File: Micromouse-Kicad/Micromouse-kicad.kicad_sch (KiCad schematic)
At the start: 101 parts, among them J1 SWD, J2 USB_B_Micro, J3 UARTBTH, J4 Batería, J5 VL6180x, J6 MotorEncodL, J7 MotorEncodR, Q1 BS170, Q2 BS170, Q3 BS170, Q4 BS170, SW1 RST, SW2 BootSwitch, SW3 PowerSwitch, SW4 BTN, SW5 BTN, U1 STM32F405RGT6, U10 TCRT5000, U2 AMS1117-5.0, U3 AMS1117-3.3, U4 SRV05-4, U5 MPU-6500, U6 DRV8833PWPR, U7 TCRT5000, U8 TCRT5000, U9 TCRT5000, Y1 8MHz

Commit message: PCB Completa - Depurada
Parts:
- removed DL1: ROJO, LED_SMD:LED_0603_1608Metric, symbol Device:LED
- removed DL3: VERDE, LED_SMD:LED_0603_1608Metric, symbol Device:LED
- removed R2: 220, Resistor_SMD:R_0603_1608Metric, symbol Device:R_Small
- removed RX1: 750, Resistor_SMD:R_0603_1608Metric, symbol Device:R_Small
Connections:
- net LED1: no longer names the net of U1.39 (PC8)
- net LED6: no longer names the net of U1.43 (PA10)
- no-connect marks 37 -> 39
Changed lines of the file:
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@@
   (no_connect (at 200.66 49.53))
   (no_connect (at 200.66 36.83))
+  (no_connect (at 114.3 81.28))
+  (no_connect (at 114.3 71.12))
   (no_connect (at 256.54 92.71))
   (no_connect (at 154.94 96.52))
@@
     )
   )
-  (global_label "LED6" (shape input) (at 114.3 81.28 0) (fields_autoplaced)
-    (effects (font (size 1.27 1.27)) (justify left))
-    (property "Intersheet References" "${INTERSHEET_REFS}" (id 0) (at 121.3698 81.2006 0)
-      (effects (font (size 1.27 1.27)) (justify left) hide)
-    )
-  )
   (global_label "Boton" (shape input) (at 83.82 83.82 180) (fields_autoplaced)
     (effects (font (size 1.27 1.27)) (justify right))
@@
     )
   )
-  (global_label "LED1" (shape input) (at 114.3 71.12 0) (fields_autoplaced)
-    (effects (font (size 1.27 1.27)) (justify left))
-    (property "Intersheet References" "${INTERSHEET_REFS}" (id 0) (at 121.3698 71.0406 0)
-      (effects (font (size 1.27 1.27)) (justify left) hide)
-    )
-  )
   (global_label "SWDIO" (shape input) (at 38.1 138.43 180) (fields_autoplaced)
     (effects (font (size 1.27 1.27)) (justify right))
@@
     )
   )
-  (global_label "LED1" (shape input) (at 17.78 177.8 90) (fields_autoplaced)
-    (effects (font (size 1.27 1.27)) (justify left))
-    (property "Intersheet References" "${INTERSHEET_REFS}" (id 0) (at 17.7006 170.7302 90)
-      (effects (font (size 1.27 1.27)) (justify left) hide)
-    )
-  )
   (global_label "OutML1" (shape input) (at 271.78 73.66 0) (fields_autoplaced)
     (effects (font (size 1.27 1.27)) (justify left))
@@
     )
   )
-  (global_label "LED6" (shape input) (at 43.18 177.8 90) (fields_autoplaced)
-    (effects (font (size 1.27 1.27)) (justify left))
-    (property "Intersheet References" "${INTERSHEET_REFS}" (id 0) (at 43.1006 170.7302 90)
-      (effects (font (size 1.27 1.27)) (justify left) hide)
-    )
-  )
   (global_label "I2C2_SCL" (shape input) (at 74.93 97.79 180) (fields_autoplaced)
     (effects (font (size 1.27 1.27)) (justify right))
@@
     (pin "2")
   )
-  (symbol (lib_id "power:GND") (at 43.18 190.5 0) (unit 1)
-    (in_bom yes) (on_board yes) (fields_autoplaced)
-    (property "Reference" "#PWR012" (id 0) (at 43.18 196.85 0)
-      (effects (font (size 1.27 1.27)) hide)
-    )
-    (property "Value" "GND" (id 1) (at 43.18 195.58 0))
-    (property "Footprint" "" (id 2) (at 43.18 190.5 0)
-      (effects (font (size 1.27 1.27)) hide)
-    )
-    (property "Datasheet" "" (id 3) (at 43.18 190.5 0)
-      (effects (font (size 1.27 1.27)) hide)
-    )
-    (pin "1")
-  )
   (symbol (lib_id "power:GND") (at 149.86 190.5 0) (unit 1)
     (in_bom yes) (on_board yes) (fields_autoplaced)
@@
     (pin "2")
   )
-  (symbol (lib_id "Device:LED") (at 43.18 186.69 90) (unit 1)
-    (in_bom yes) (on_board yes)
-    (property "Reference" "DL3" (id 0) (at 46.99 187.0074 90)
-      (effects (font (size 1.27 1.27)) (justify right))
-    )
-    (property "Value" "VERDE" (id 1) (at 46.99 189.5474 90)
-      (effects (font (size 1.27 1.27)) (justify right))
-    )
-    (property "Footprint" "LED_SMD:LED_0603_1608Metric" (id 2) (at 43.18 186.69 0)
-      (effects (font (size 1.27 1.27)) hide)
-    )
-    (property "Datasheet" "~" (id 3) (at 43.18 186.69 0)
-      (effects (font (size 1.27 1.27)) hide)
-    )
-    (pin "1")
-    (pin "2")
-  )
   (symbol (lib_id "Device:C_Small") (at 16.51 27.94 0) (unit 1)
     (in_bom yes) (on_board yes) (fields_autoplaced)
@@
     (pin "9")
   )
-  (symbol (lib_id "Device:R_Small") (at 43.18 180.34 0) (unit 1)
-    (in_bom yes) (on_board yes) (fields_autoplaced)
-    (property "Reference" "R2" (id 0) (at 45.72 179.0699 0)
-      (effects (font (size 1.27 1.27)) (justify left))
-    )
-    (property "Value" "220" (id 1) (at 45.72 181.6099 0)
-      (effects (font (size 1.27 1.27)) (justify left))
-    )
-    (property "Footprint" "Resistor_SMD:R_0603_1608Metric" (id 2) (at 43.18 180.34 0)
-      (effects (font (size 1.27 1.27)) hide)
-    )
-    (property "Datasheet" "~" (id 3) (at 43.18 180.34 0)
-      (effects (font (size 1.27 1.27)) hide)
-    )
-    (pin "1")
-    (pin "2")
-  )
   (symbol (lib_id "power:+3.3V") (at 260.35 119.38 0) (unit 1)
     (in_bom yes) (on_board yes) (fields_autoplaced)
@@
     (pin "2")
   )
-  (symbol (lib_id "Device:R_Small") (at 17.78 180.34 0) (unit 1)
-    (in_bom yes) (on_board yes) (fields_autoplaced)
-    (property "Reference" "RX1" (id 0) (at 20.32 179.0699 0)
-      (effects (font (size 1.27 1.27)) (justify left))
-    )
-    (property "Value" "750" (id 1) (at 20.32 181.6099 0)
-      (effects (font (size 1.27 1.27)) (justify left))
-    )
-    (property "Footprint" "Resistor_SMD:R_0603_1608Metric" (id 2) (at 17.78 180.34 0)
-      (effects (font (size 1.27 1.27)) hide)
-    )
-    (property "Datasheet" "~" (id 3) (at 17.78 180.34 0)
-      (effects (font (size 1.27 1.27)) hide)
-    )
-    (pin "1")
-    (pin "2")
-  )
   (symbol (lib_id "power:GND") (at 285.75 170.18 270) (unit 1)
     (in_bom yes) (on_board yes) (fields_autoplaced)
@@
     (pin "1")
   )
-  (symbol (lib_id "power:GND") (at 17.78 190.5 0) (unit 1)
-    (in_bom yes) (on_board yes) (fields_autoplaced)
-    (property "Reference" "#PWR02" (id 0) (at 17.78 196.85 0)
-      (effects (font (size 1.27 1.27)) hide)
-    )
-    (property "Value" "GND" (id 1) (at 17.78 195.58 0))
-    (property "Footprint" "" (id 2) (at 17.78 190.5 0)
-      (effects (font (size 1.27 1.27)) hide)
-    )
-    (property "Datasheet" "" (id 3) (at 17.78 190.5 0)
-      (effects (font (size 1.27 1.27)) hide)
-    )
-    (pin "1")
-  )
   (symbol (lib_id "power:VAA") (at 209.55 173.99 270) (unit 1)
     (in_bom yes) (on_board yes) (fields_autoplaced)
@@
     (pin "1")
   )
-  (symbol (lib_id "Device:LED") (at 17.78 186.69 90) (unit 1)
-    (in_bom yes) (on_board yes) (fields_autoplaced)
-    (property "Reference" "DL1" (id 0) (at 21.59 187.0074 90)
-      (effects (font (size 1.27 1.27)) (justify right))
-    )
-    (property "Value" "ROJO" (id 1) (at 21.59 189.5474 90)
-      (effects (font (size 1.27 1.27)) (justify right))
-    )
-    (property "Footprint" "LED_SMD:LED_0603_1608Metric" (id 2) (at 17.78 186.69 0)
-      (effects (font (size 1.27 1.27)) hide)
-    )
-    (property "Datasheet" "~" (id 3) (at 17.78 186.69 0)
-      (effects (font (size 1.27 1.27)) hide)
-    )
-    (pin "1")
-    (pin "2")
-  )
   (symbol (lib_id "power:+3.3V") (at 410.21 85.09 0) (unit 1)
     (in_bom yes) (on_board yes) (fields_autoplaced)
@@
       (reference "#PWR01") (unit 1) (value "+3.3V") (footprint "")
     )
-    (path "/be344b93-f0c0-489b-b68e-ea1eb4ebd301"
-      (reference "#PWR02") (unit 1) (value "GND") (footprint "")
-    )
     (path "/8d533f32-19b8-4d37-9b18-85480ab04d92"
       (reference "#PWR03") (unit 1) (value "+3.3V") (footprint "")
@@
       (reference "#PWR011") (unit 1) (value "GND") (footprint "")
     )
-    (path "/09b16a4c-98eb-4a63-a90c-d7792ed4bea8"
-      (reference "#PWR012") (unit 1) (value "GND") (footprint "")
-    )
     (path "/e1aec55e-33df-471e-82f8-1ffd557fcb18"
       (reference "#PWR013") (unit 1) (value "GND") (footprint "")
@@
       (reference "D2") (unit 1) (value "B5819W") (footprint "Diode_SMD:D_SOD-123")
     )
-    (path "/e6712806-8c22-44f2-bf7d-4a2d10fe6d5c"
-      (reference "DL1") (unit 1) (value "ROJO") (footprint "LED_SMD:LED_0603_1608Metric")
-    )
     (path "/7134e756-0a61-443f-bb6d-fecdd623881a"
       (reference "DL2") (unit 1) (value "AZUL") (footprint "LED_SMD:LED_0603_1608Metric")
     )
-    (path "/4600a087-6880-437d-af91-1e84be1a1d53"
-      (reference "DL3") (unit 1) (value "VERDE") (footprint "LED_SMD:LED_0603_1608Metric")
-    )
     (path "/5fbf1597-61af-4c6c-89a9-660ed6185769"
       (reference "DL7") (unit 1) (value "VERDE") (footprint "LED_SMD:LED_0603_1608Metric")
@@
       (reference "R1") (unit 1) (value "220") (footprint "Resistor_SMD:R_0603_1608Metric")
     )
-    (path "/86c5061d-8e09-4bab-b0e5-86f6707d9e5e"
-      (reference "R2") (unit 1) (value "220") (footprint "Resistor_SMD:R_0603_1608Metric")
-    )
     (path "/45c613f9-aec8-424a-b480-e2cd3c7f1c41"
       (reference "R4") (unit 1) (value "220") (footprint "Resistor_SMD:R_0603_1608Metric")
@@
       (reference "RU3") (unit 1) (value "22") (footprint "Resistor_SMD:R_0603_1608Metric")
     )
-    (path "/a5ccd16c-0207-46ed-a536-7bf8b96e3f2b"
-      (reference "RX1") (unit 1) (value "750") (footprint "Resistor_SMD:R_0603_1608Metric")
-    )
     (path "/904ae360-b03d-4f3f-a237-22e33f2af105"

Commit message: Modelo 3D
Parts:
- J6, J7: footprint Connector_JST:JST_XH_B6B-XH-A_1x06_P2.50mm_Vertical -> Connector_JST:JST_SHL_SM06B-SHLS-TF_1x06-1MP_P1.00mm_Horizontal
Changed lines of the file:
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@@
       (effects (font (size 1.27 1.27)) (justify left))
     )
-    (property "Footprint" "Connector_JST:JST_XH_B6B-XH-A_1x06_P2.50mm_Vertical" (id 2) (at 290.83 175.26 0)
+    (property "Footprint" "Connector_JST:JST_SHL_SM06B-SHLS-TF_1x06-1MP_P1.00mm_Horizontal" (id 2) (at 290.83 175.26 0)
       (effects (font (size 1.27 1.27)) hide)
     )
@@
       (effects (font (size 1.27 1.27)) (justify left))
     )
-    (property "Footprint" "Connector_JST:JST_XH_B6B-XH-A_1x06_P2.50mm_Vertical" (id 2) (at 256.54 175.26 0)
+    (property "Footprint" "Connector_JST:JST_SHL_SM06B-SHLS-TF_1x06-1MP_P1.00mm_Horizontal" (id 2) (at 256.54 175.26 0)
       (effects (font (size 1.27 1.27)) hide)
     )
@@
     )
     (path "/6b173ad2-a80e-42b7-b9a4-03e34411ed68"
-      (reference "J6") (unit 1) (value "MotorEncodL") (footprint "Connector_JST:JST_XH_B6B-XH-A_1x06_P2.50mm_Vertical")
+      (reference "J6") (unit 1) (value "MotorEncodL") (footprint "Connector_JST:JST_SHL_SM06B-SHLS-TF_1x06-1MP_P1.00mm_Horizontal")
     )
     (path "/2301f17e-45ec-4ade-8b9e-4d97bea85791"
-      (reference "J7") (unit 1) (value "MotorEncodR") (footprint "Connector_JST:JST_XH_B6B-XH-A_1x06_P2.50mm_Vertical")
+      (reference "J7") (unit 1) (value "MotorEncodR") (footprint "Connector_JST:JST_SHL_SM06B-SHLS-TF_1x06-1MP_P1.00mm_Horizontal")
     )
     (path "/3263ba06-1178-4ee5-967f-6cb2162e5cc6"

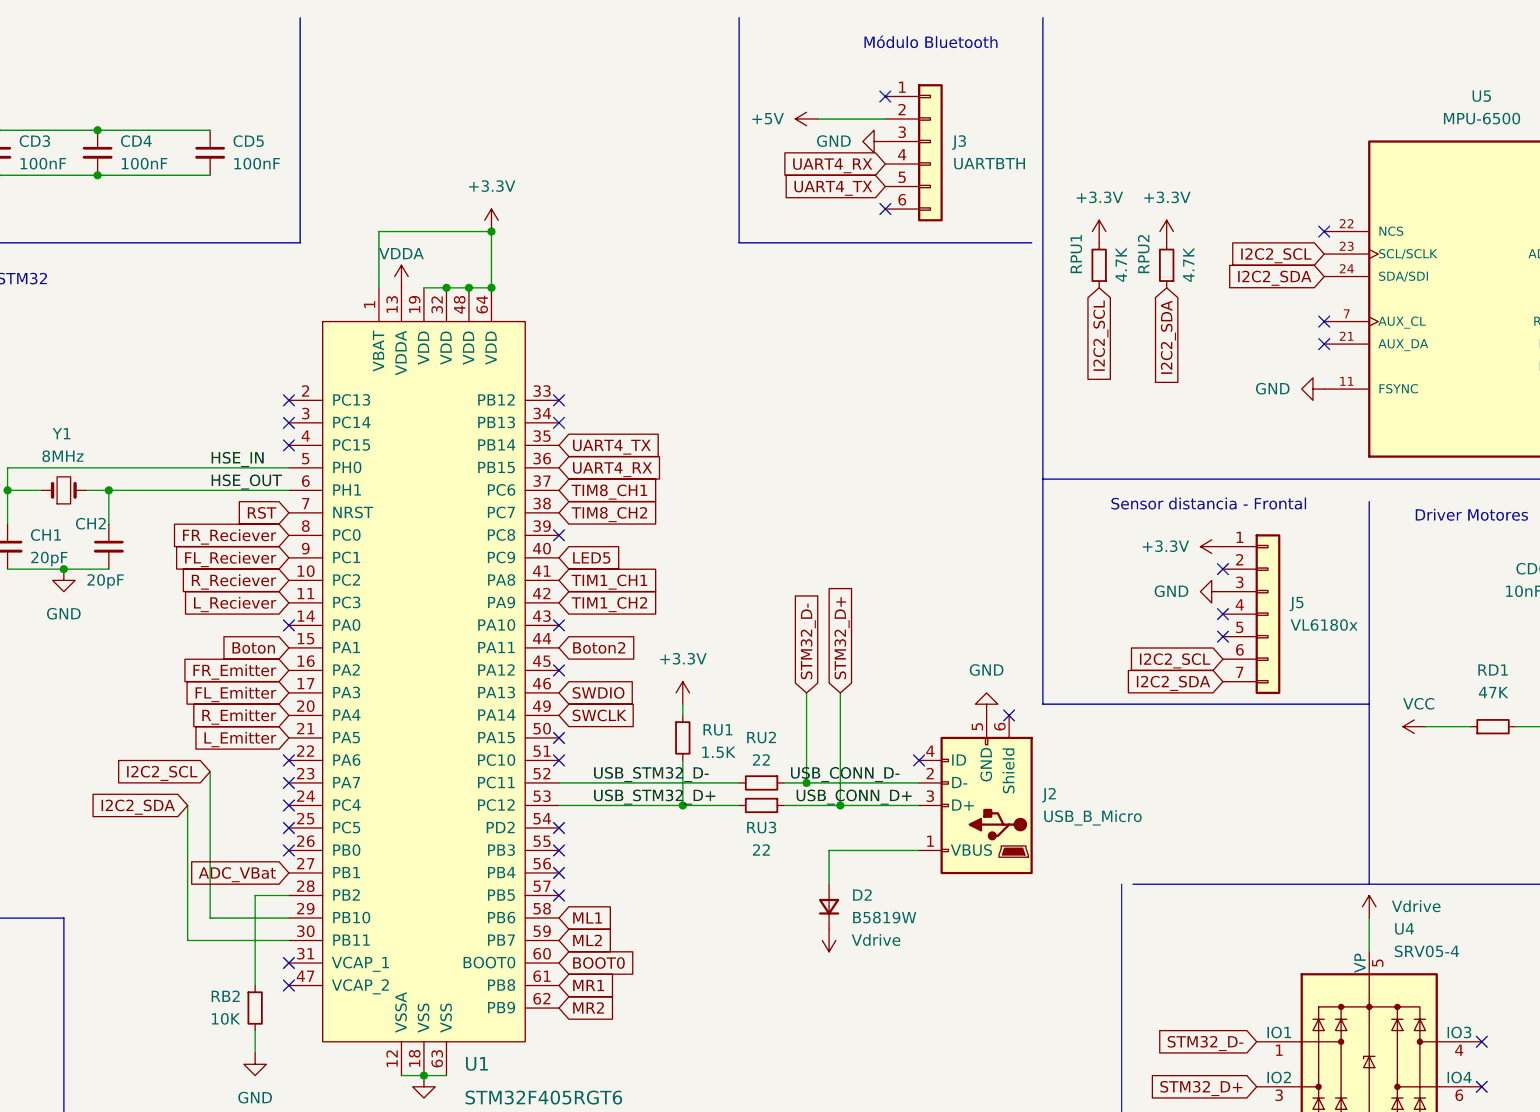
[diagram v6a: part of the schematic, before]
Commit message: Vias y caminos borrados
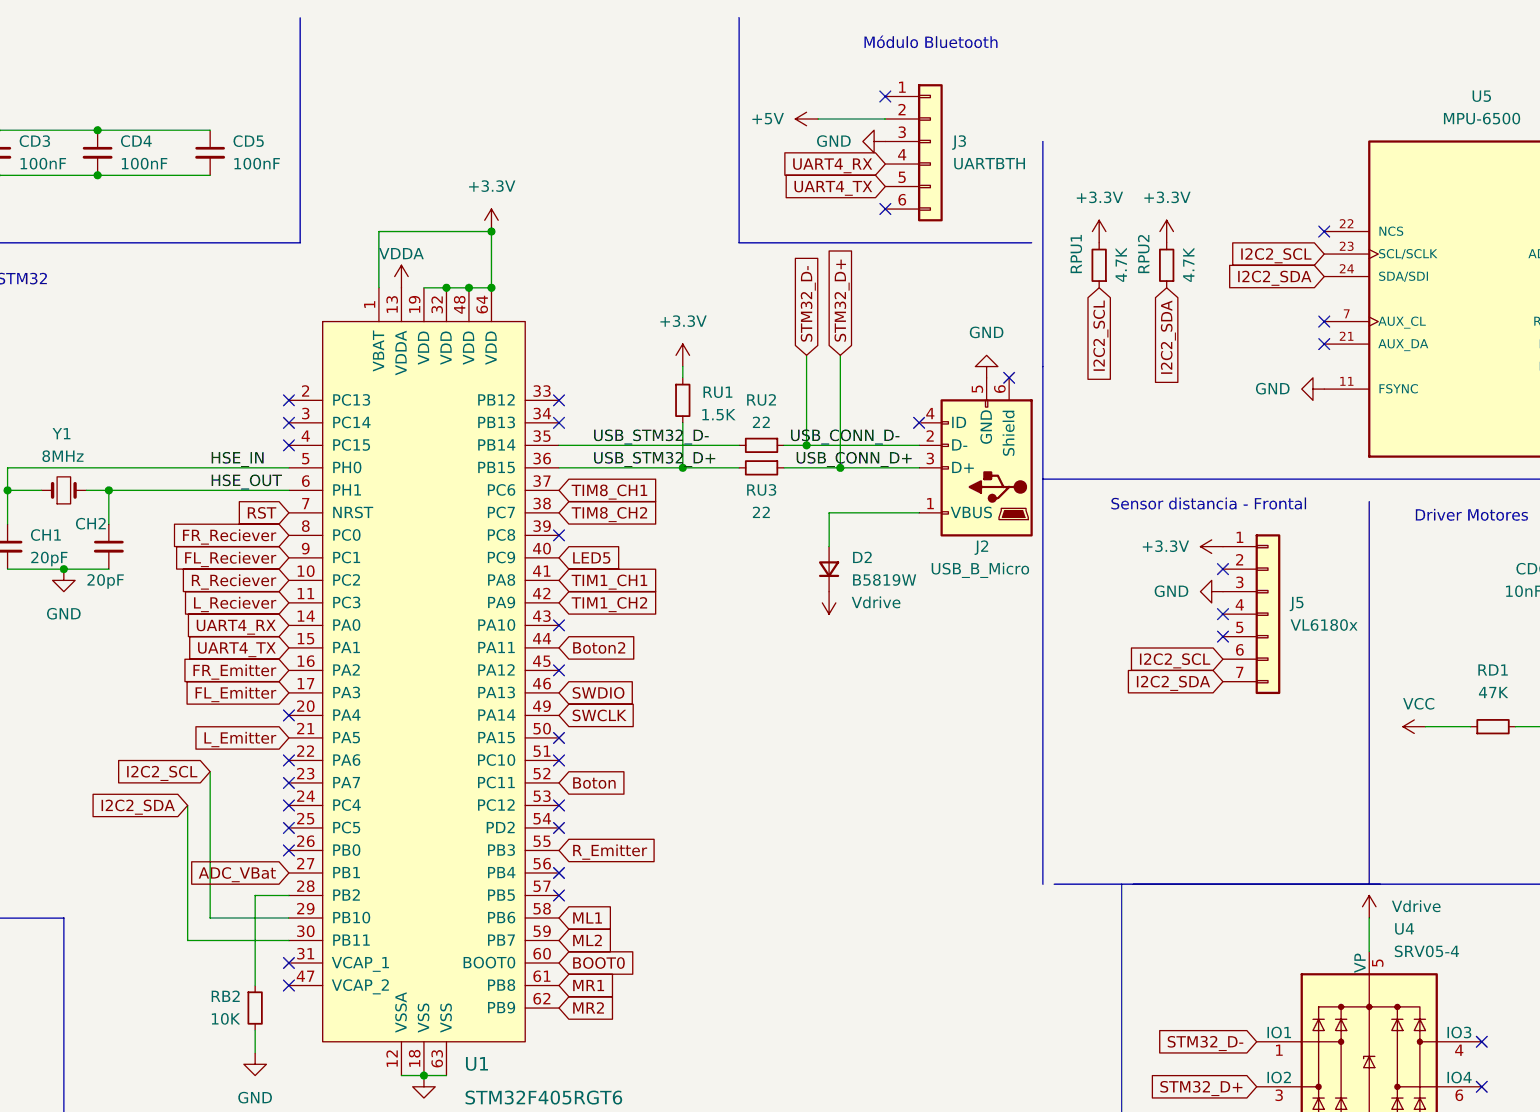
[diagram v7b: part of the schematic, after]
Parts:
- J6, J7: footprint Connector_JST:JST_SHL_SM06B-SHLS-TF_1x06-1MP_P1.00mm_Horizontal -> Connector_JST:JST_SH_BM06B-SRSS-TB_1x06-1MP_P1.00mm_Vertical
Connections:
- net Boton: now also U1.52 (PC11); no longer U1.15 (PA1)
- net R_Emitter: now also U1.55 (PB3); no longer U1.20 (PA4)
- net UART4_RX: now also U1.14 (PA0); no longer U1.36 (PB15)
- net UART4_TX: now also U1.15 (PA1); no longer U1.35 (PB14)
- net USB_STM32_D+: now also U1.36 (PB15); no longer U1.53 (PC12)
- net USB_STM32_D-: now also U1.35 (PB14); no longer U1.52 (PC11)
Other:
- moved on the sheet: D2, J2, RU1, RU2, RU3

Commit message: Blackpill incluida
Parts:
- removed CBOT2, CD1, CD2, CD3, CD4, CD5, CF2, CP1, CRST1: 100nF, Capacitor_SMD:C_0402_1005Metric, symbol Device:C_Small
- removed CDR1: 4.7uF, Capacitor_SMD:C_0402_1005Metric, symbol Device:C_Small
- removed CF1: 1uF, Capacitor_SMD:C_0402_1005Metric, symbol Device:C_Small
- removed CH1, CH2: 20pF, Capacitor_SMD:C_0402_1005Metric, symbol Device:C_Small
- removed D1, D2: B5819W, Diode_SMD:D_SOD-123, symbol Device:D_Small
- removed J1: SWD, Connector_PinHeader_2.54mm:PinHeader_1x04_P2.54mm_Vertical, symbol Connector_Generic:Conn_01x04
- removed J2: USB_B_Micro, HUELLAS:MICRO-USB-SMD_5P-P0.65-H-F_MICRO5.9MMUSB, symbol Connector:USB_B_Micro
- removed LF1: 27nH, Inductor_SMD:L_0402_1005Metric, symbol Device:L_Small
- removed RB1, RB2, RBOT2, RRST1: 10K, Resistor_SMD:R_0402_1005Metric, symbol Device:R_Small
- removed RU1: 1.5K, Resistor_SMD:R_0402_1005Metric, symbol Device:R_Small
- removed RU2, RU3: 22, Resistor_SMD:R_0603_1608Metric, symbol Device:R_Small
- removed SW1: RST, Button_Switch_THT:SW_PUSH_6mm_H5mm, symbol Switch:SW_Push
- removed SW2: BootSwitch, HUELLAS:Switch_Slide, symbol Switch:SW_Push_SPDT
- removed SW5: BTN, Button_Switch_THT:SW_PUSH_6mm_H5mm, symbol Switch:SW_Push
- removed U1: STM32F405RGT6, digikey-footprints:LQFP-64_10x10mm, symbol dk_Embedded-Microcontrollers:STM32F405RGT6
- removed U4: SRV05-4, Package_TO_SOT_SMD:SOT-23-6, symbol Power_Protection:SRV05-4
- removed Y1: 8MHz, Crystal:Crystal_SMD_5032-2Pin_5.0x3.2mm, symbol Device:Crystal_Small
- added U1: YAAJ_WeAct_BlackPill_Part_Like, FootprintSTM32Nucleo:Blackpill2, symbol STM32:YAAJ_WeAct_BlackPill_Part_Like
- renumbered CD6 to CD1, CD7 to CD2, DL2 to DL1, DL7 to DL2, J3 to J1, J4 to J2, J5 to J3, J6 to J4, J7 to J5, R12 to R10, R13 to R11, R14 to R12, R15 to R13, R16 to R14, R17 to R15, R18 to R16, R19 to R17, R20 to R18, R4 to R2, R5 to R3, R6 to R4, R7 to R5, R8 to R6, R9 to R7, R10 to R8, R11 to R9, SW3 to SW1, SW4 to SW2, U5 to U4, U6 to U5, U7 to U6, U8 to U7, U9 to U8, U10 to U9
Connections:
- net +3.3V: now also U1.20 (3V3), U1.38 (3V3)
- net ADC_VBat: now also U1.30 (PA4)
- net Boton: now also U1.1 (PB12)
- net FL_Emitter: now also U1.11 (PB3)
- net FL_Reciever: now also U1.35 (PB1)
- net FR_Emitter: now also U1.10 (PA15)
- net FR_Reciever: now also U1.34 (PB0)
- net GND: now also J2.2 (Pin_2), U1.19 (GND), U1.39 (GND); no longer J2.1 (Pin_1)
- net I2C2_SCL: now also U1.16 (PB8)
- net I2C2_SDA: now also U1.17 (PB9)
- net LED5: now also U1.2 (PB13)
- net L_Emitter: now also U1.13 (PB5)
- net L_Reciever: now also U1.26 (PA0)
- net ML1: now also U1.5 (PA8)
- net ML2: now also U1.6 (PA9)
- net MR1: now also U1.7 (PA10)
- net MR2: now also U1.37 (PB10)
- net R_Emitter: now also U1.12 (PB4)
- net R_Reciever: now also U1.27 (PA1)
- net UART4_RX: now also U1.28 (PA2)
- net UART4_TX: now also U1.29 (PA3)
- net VAA: now also J2.1 (Pin_1); no longer J2.2 (Pin_2)
- net Vdrive: now also U1.18 (5V), U1.40 (5V)
- net TIM1_CH1 renamed TIM4_CH1
- net TIM4_CH1: now also U1.14 (PB6)
- net TIM1_CH2 renamed TIM4_CH2
- net TIM4_CH2: now also U1.15 (PB7)
- net TIM8_CH1 renamed TIM3_CH1
- net TIM3_CH1: now also U1.32 (PA6)
- net TIM8_CH2 renamed TIM3_CH2
- net TIM3_CH2: now also U1.33 (PA7)
- no-connect marks 39 -> 24
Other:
- note removed: "Boot Set-up y programación"
- note removed: "Botón Extra 2"
- note removed: "Botón de Reset"
- note removed: "Capacitancias de desacople"
- note removed: "Filtro Pasa-Bajas 1MHz (Alimentación de pines análogos)"
- note removed: "Protección USB"
